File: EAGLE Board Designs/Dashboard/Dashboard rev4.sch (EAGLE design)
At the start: 97 parts, among them J1 CONNECTOR-AVR-ISP_2X05_SMD, J2 CONNECTOR-6_μF_S_RA_, J3 CONNECTOR-CAN_μF_S_RA_, J4 CONNECTOR-8_μF_S_RA_, J5 JUMPER_0603_, Q1 TRANSISTOR_N_MOS__PMV15ENEA, Q2 TRANSISTOR_N_MOS__PMV15ENEA, Q3 TRANSISTOR_N_MOS__PMV15ENEA, Q4 TRANSISTOR_N_MOS__PMV15ENEA, Q5 TRANSISTOR_N_MOS__PMV15ENEA, Q6 TRANSISTOR_N_MOS__PMV15ENEA, Q7 TRANSISTOR_N_MOS__PMV15ENEA, Q8 TRANSISTOR_N_MOS__PMV15ENEA, U1 ATMEGA328P-AU, U2 RE46C100, U3 MCP23S08, U4 MCP2562FD, U5 MCP2515, X1 CRYSTAL_16MHZ, X2 CRYSTAL_16MHZ

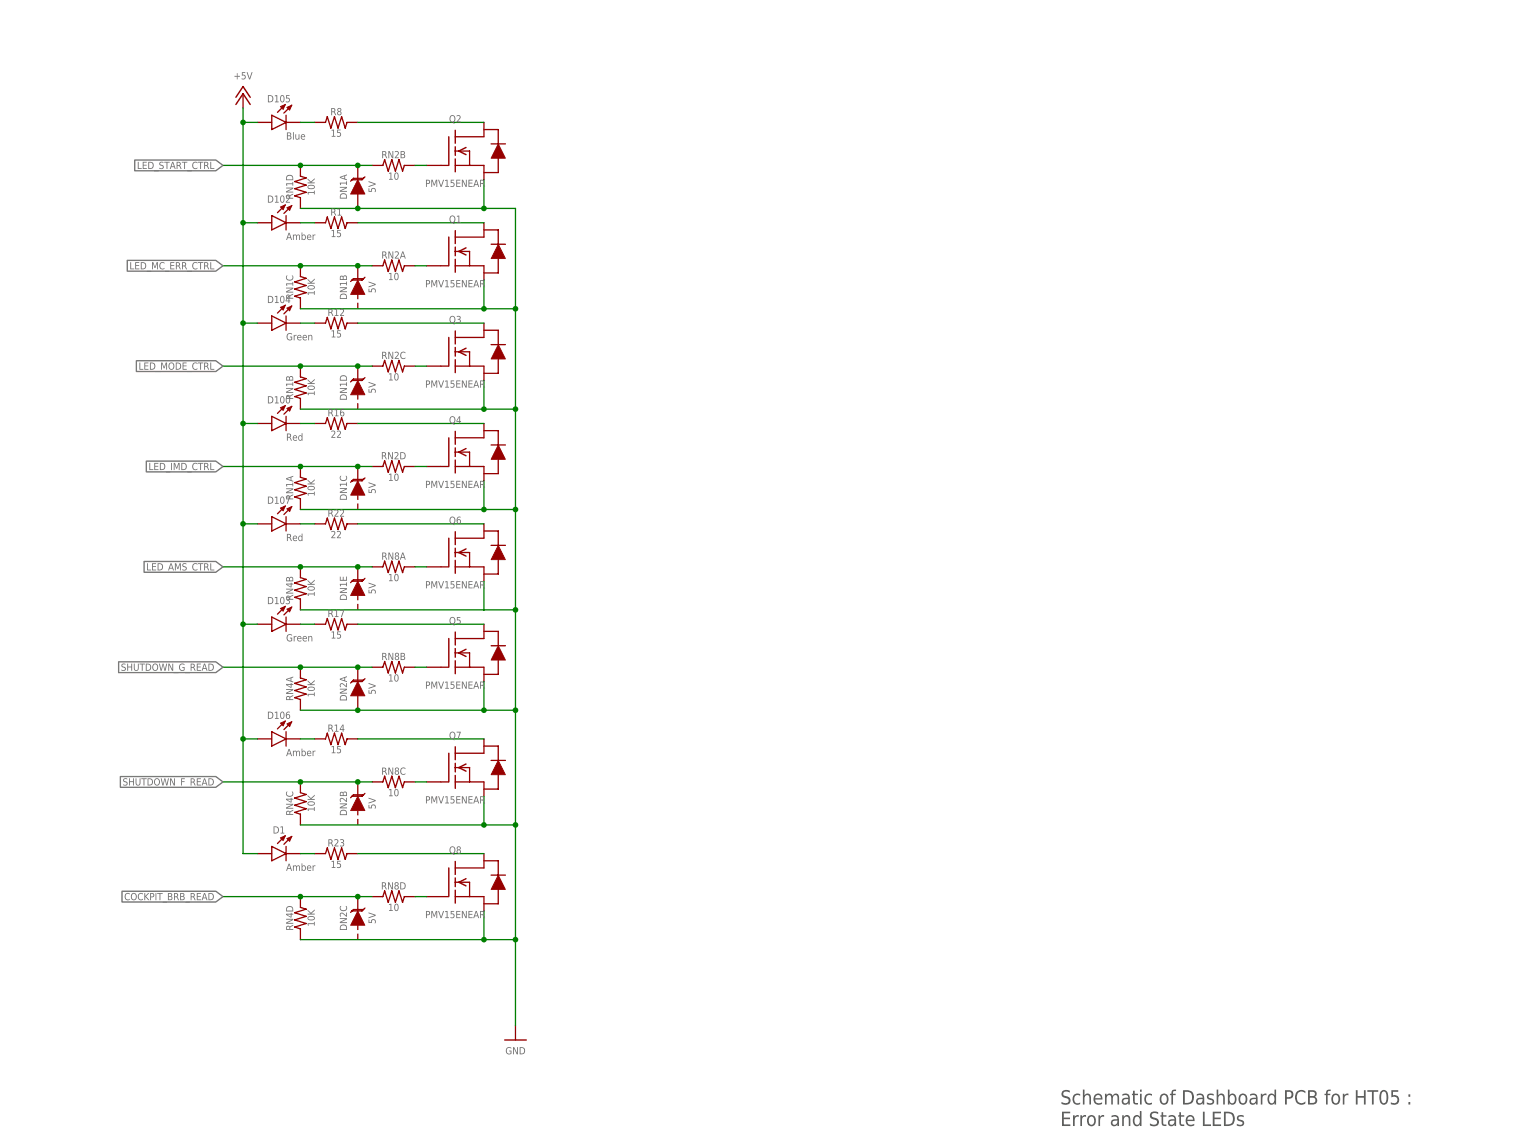
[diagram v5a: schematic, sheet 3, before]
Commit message: Updated routing and TP naming
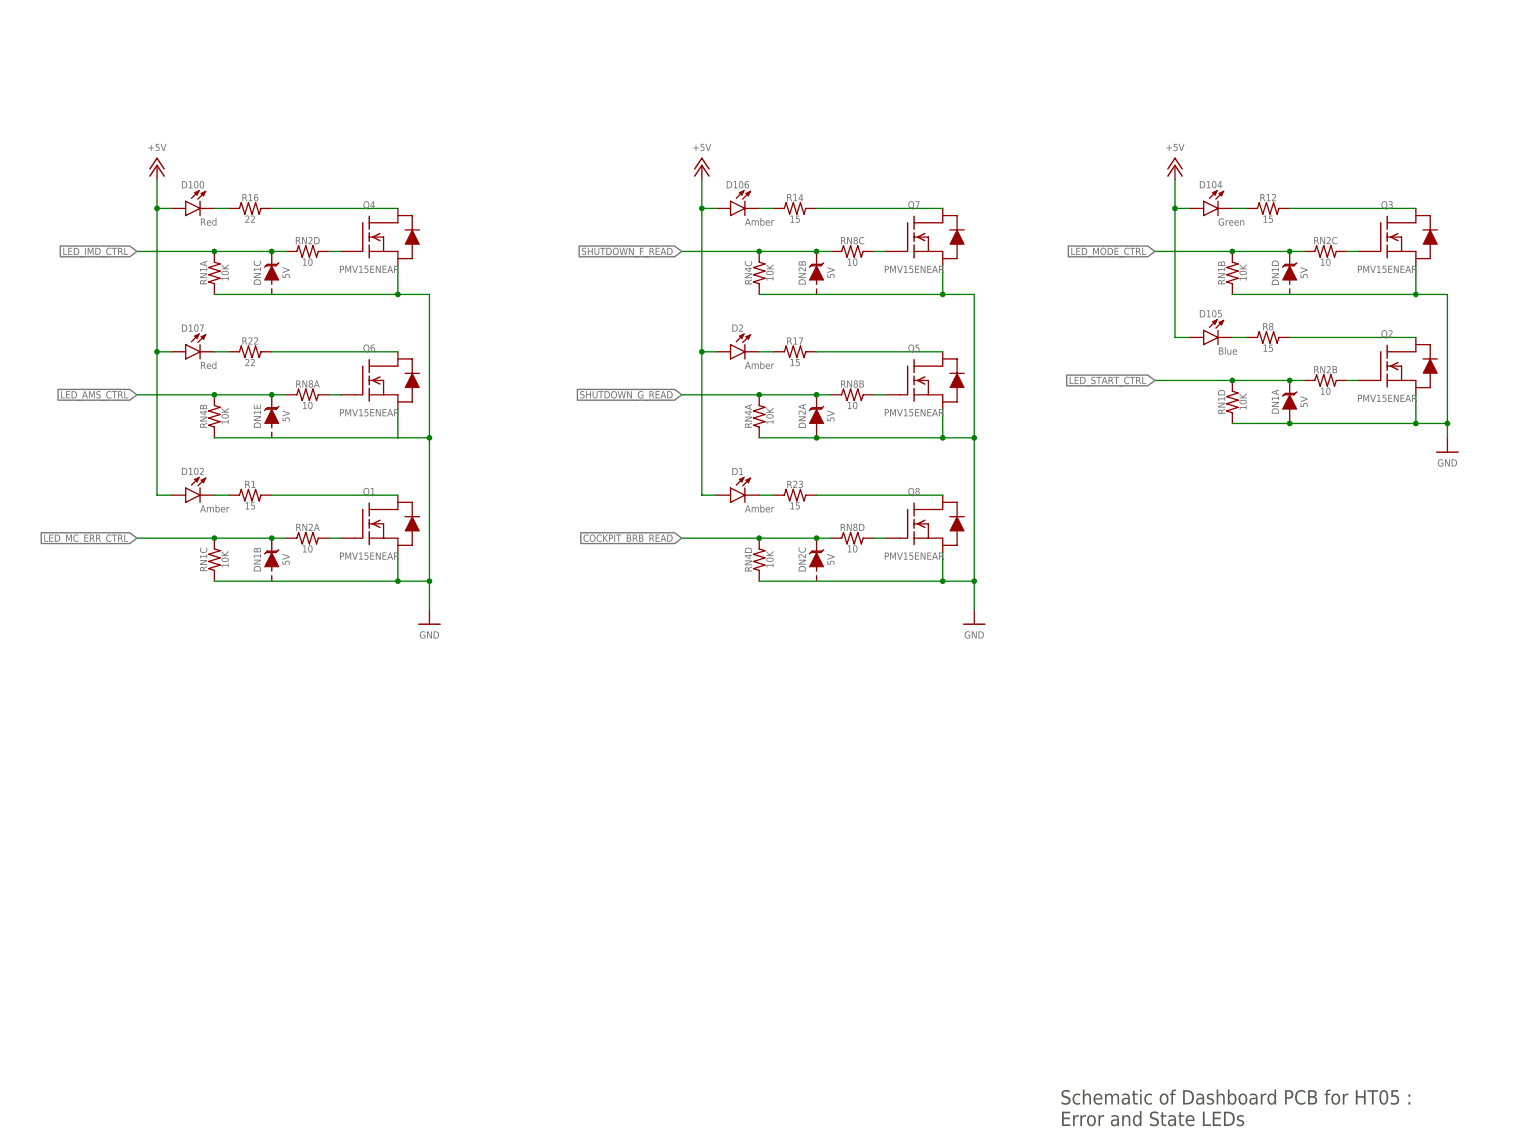
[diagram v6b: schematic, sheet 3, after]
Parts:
- removed D103: LED_2835_GREEN, HyTechDevices:LED_2835_GREEN
- added D2: LED_2835_AMBER, HyTechDevices:LED_2835_AMBER
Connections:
- net +5V: now also D2.A; no longer D103.A
- net N$40: now also D2.C; no longer D103.C
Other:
- moved on the sheet: D1, D100, D102, D104, D105, D106, D107, DN1A, DN1B, DN1C, DN1D, DN1E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

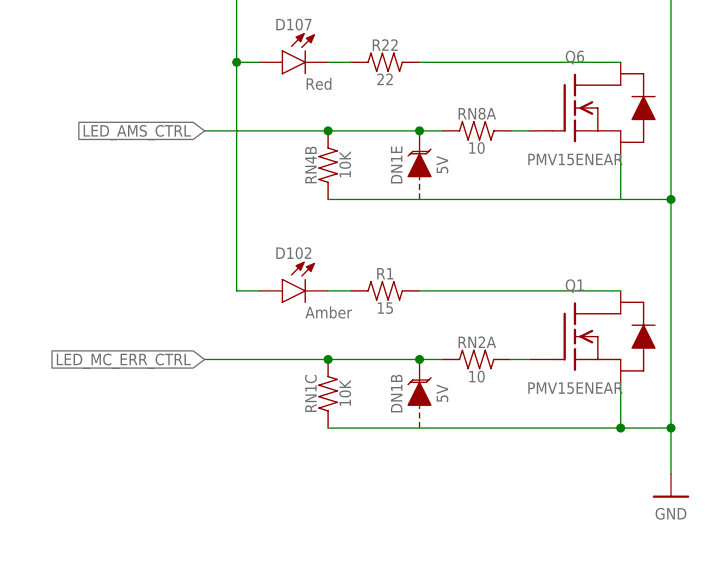
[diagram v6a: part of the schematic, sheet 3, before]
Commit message: Added red-orange led for mcu led
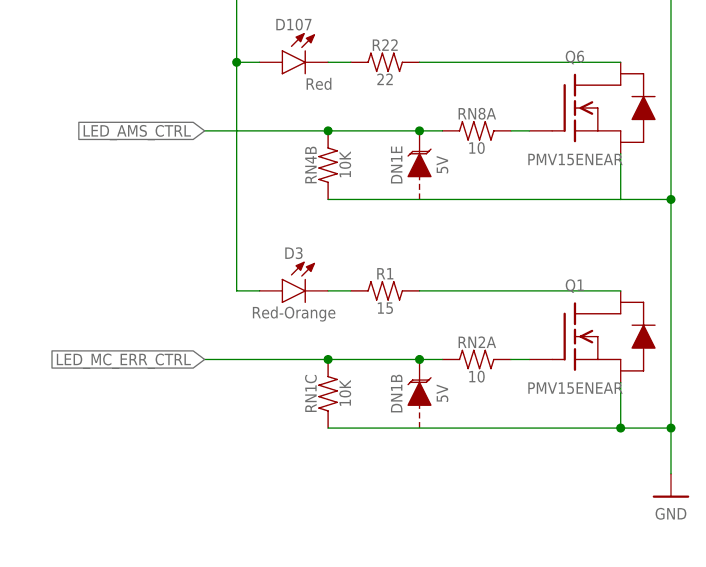
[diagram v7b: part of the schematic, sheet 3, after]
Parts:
- removed D102: LED_2835_AMBER, HyTechDevices:LED_2835_AMBER
- added D3: LED_2835_RED-ORANGE, HyTechDevices:LED_2835_RED-ORANGE
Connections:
- net +5V: now also D3.A; no longer D102.A
- net N$2: now also D3.C; no longer D102.C
- net N$41: now also J5.2; no longer J5.P$2
- net N$51: now also J5.1; no longer J5.P$1
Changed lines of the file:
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@@
 <part name="D5" library="HyTechDevices" deviceset="LED_?_*" device="0603" technology="ORANGE"/>
 <part name="RN6" library="HyTechDevices" deviceset="RESISTOR_NETWORK_4_*" device="" technology="1K"/>
-<part name="D102" library="HyTechDevices" deviceset="LED_?_*" device="2835" technology="AMBER"/>
 <part name="C10" library="HyTechDevices" deviceset="CAPACITOR_?_*" device="0603" technology="10V_0.1UF"/>
 <part name="C11" library="HyTechDevices" deviceset="CAPACITOR_?_*" device="0603" technology="10V_0.1UF"/>
@@
 <part name="P48" library="HyTechSupplies" deviceset="+5V" device=""/>
 <part name="P49" library="HyTechSupplies" deviceset="+5V" device=""/>
+<part name="D3" library="HyTechDevices" deviceset="LED_?_*" device="2835" technology="RED-ORANGE"/>
 </parts>
 <sheets>
@@
 <pinref part="R20" gate="G$1" pin="2"/>
 <wire x1="220.98" y1="154.94" x2="220.98" y2="152.4" width="0.1524" layer="91"/>
-<pinref part="J5" gate="G$1" pin="P$1"/>
+<pinref part="J5" gate="G$1" pin="1"/>
 </segment>
 </net>
@@
 <junction x="220.98" y="165.1"/>
 <pinref part="U4" gate="G$1" pin="RXD"/>
-<pinref part="J5" gate="G$1" pin="P$2"/>
+<pinref part="J5" gate="G$1" pin="2"/>
 </segment>
 </net>
@@
 <attribute name="RESISTANCE" x="158.75" y="140.97" size="1.27" layer="96" align="top-center"/>
 </instance>
-<instance part="D102" gate="LED" x="43.18" y="124.46" smashed="yes">
-<attribute name="COLOR" x="43.18" y="122.682" size="1.27" layer="95" align="top-left"/>
-<attribute name="NAME" x="41.91" y="128.016" size="1.27" layer="96" align="bottom-center"/>
-</instance>
 <instance part="DN1" gate="E" x="55.88" y="139.7" smashed="yes" rot="R90">
 <attribute name="NAME" x="53.975" y="138.43" size="1.27" layer="95" rot="R90" align="bottom-center"/>
@@
 <instance part="P49" gate="1" x="215.9" y="182.88" smashed="yes">
 <attribute name="VALUE" x="215.9" y="185.42" size="1.27" layer="96" align="bottom-center"/>
+</instance>
+<instance part="D3" gate="LED" x="43.18" y="124.46" smashed="yes">
+<attribute name="COLOR" x="41.91" y="122.682" size="1.27" layer="95" align="top-center"/>
+<attribute name="NAME" x="41.91" y="128.016" size="1.27" layer="96" align="bottom-center"/>
 </instance>
 </instances>
@@
 <segment>
 <wire x1="48.26" y1="124.46" x2="45.72" y2="124.46" width="0.1524" layer="91"/>
-<pinref part="D102" gate="LED" pin="C"/>
 <pinref part="R1" gate="G$1" pin="1"/>
+<pinref part="D3" gate="LED" pin="C"/>
 </segment>
 </net>
@@
 <wire x1="35.56" y1="175.26" x2="35.56" y2="149.86" width="0.1524" layer="91"/>
 <junction x="35.56" y="175.26"/>
-<pinref part="D102" gate="LED" pin="A"/>
 <wire x1="38.1" y1="124.46" x2="35.56" y2="124.46" width="0.1524" layer="91"/>
 <wire x1="35.56" y1="149.86" x2="35.56" y2="124.46" width="0.1524" layer="91"/>
 <junction x="35.56" y="149.86"/>
-</segment>
-<segment>
+<pinref part="D3" gate="LED" pin="A"/>
+</segment>
+<segment>

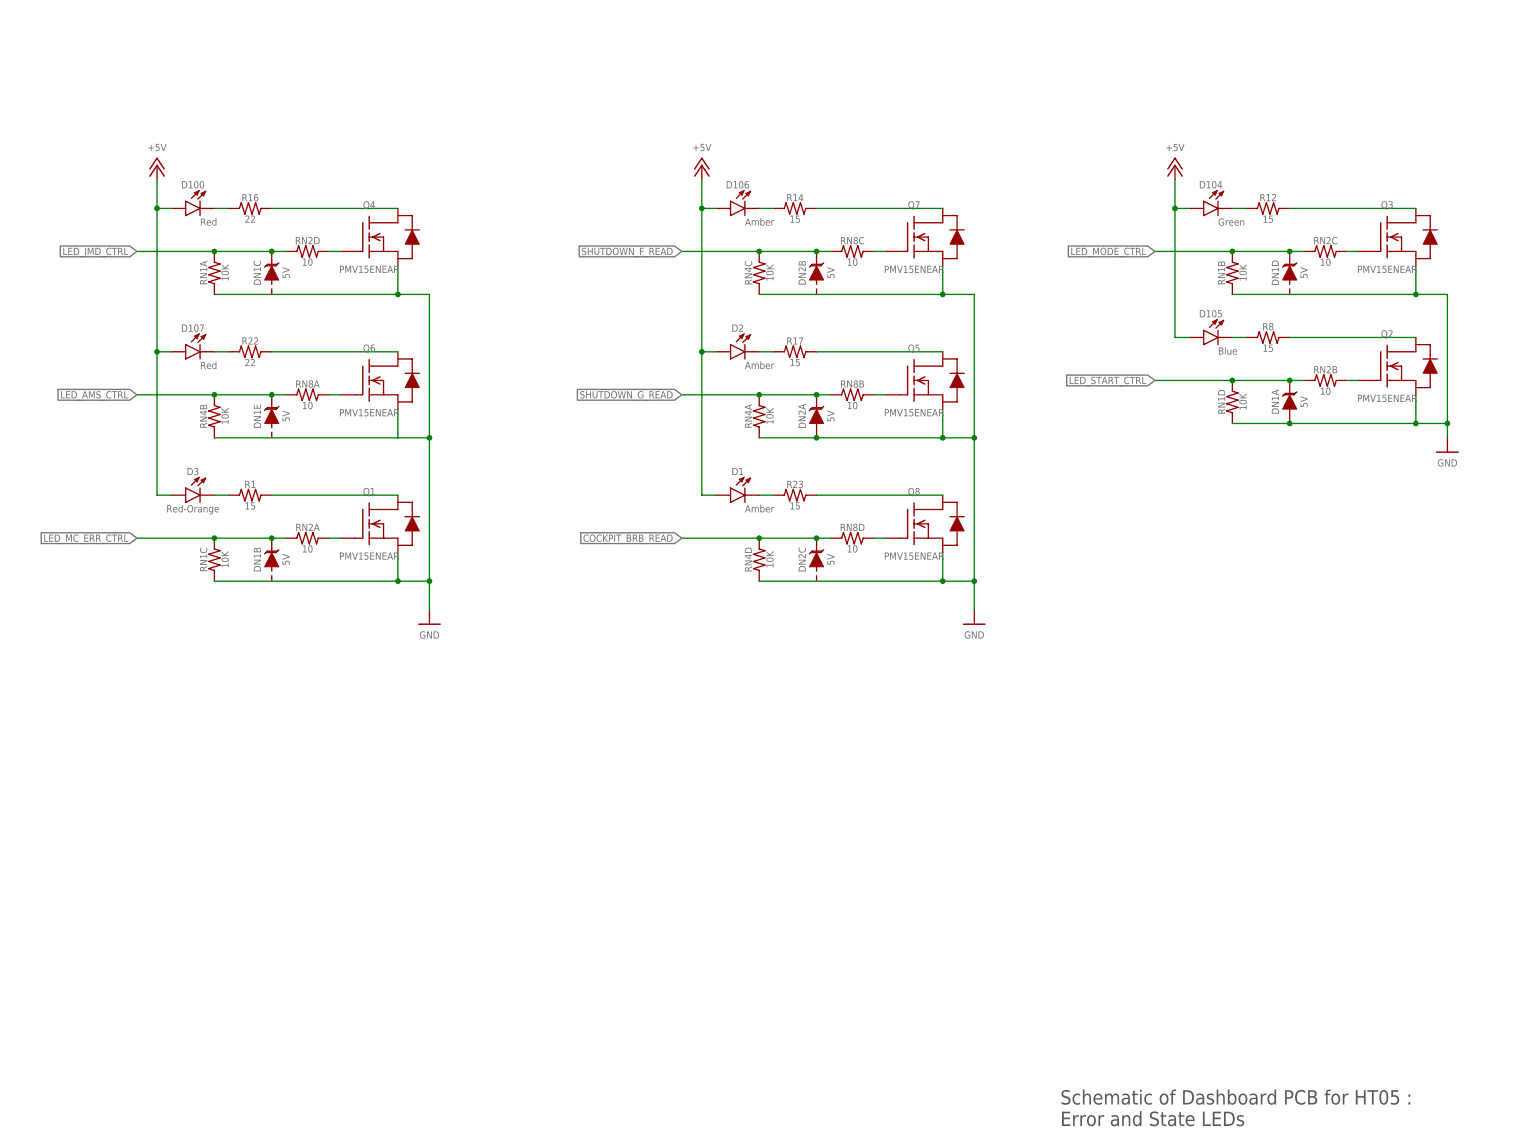
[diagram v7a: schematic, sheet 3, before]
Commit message: Added not gates and tractive LED
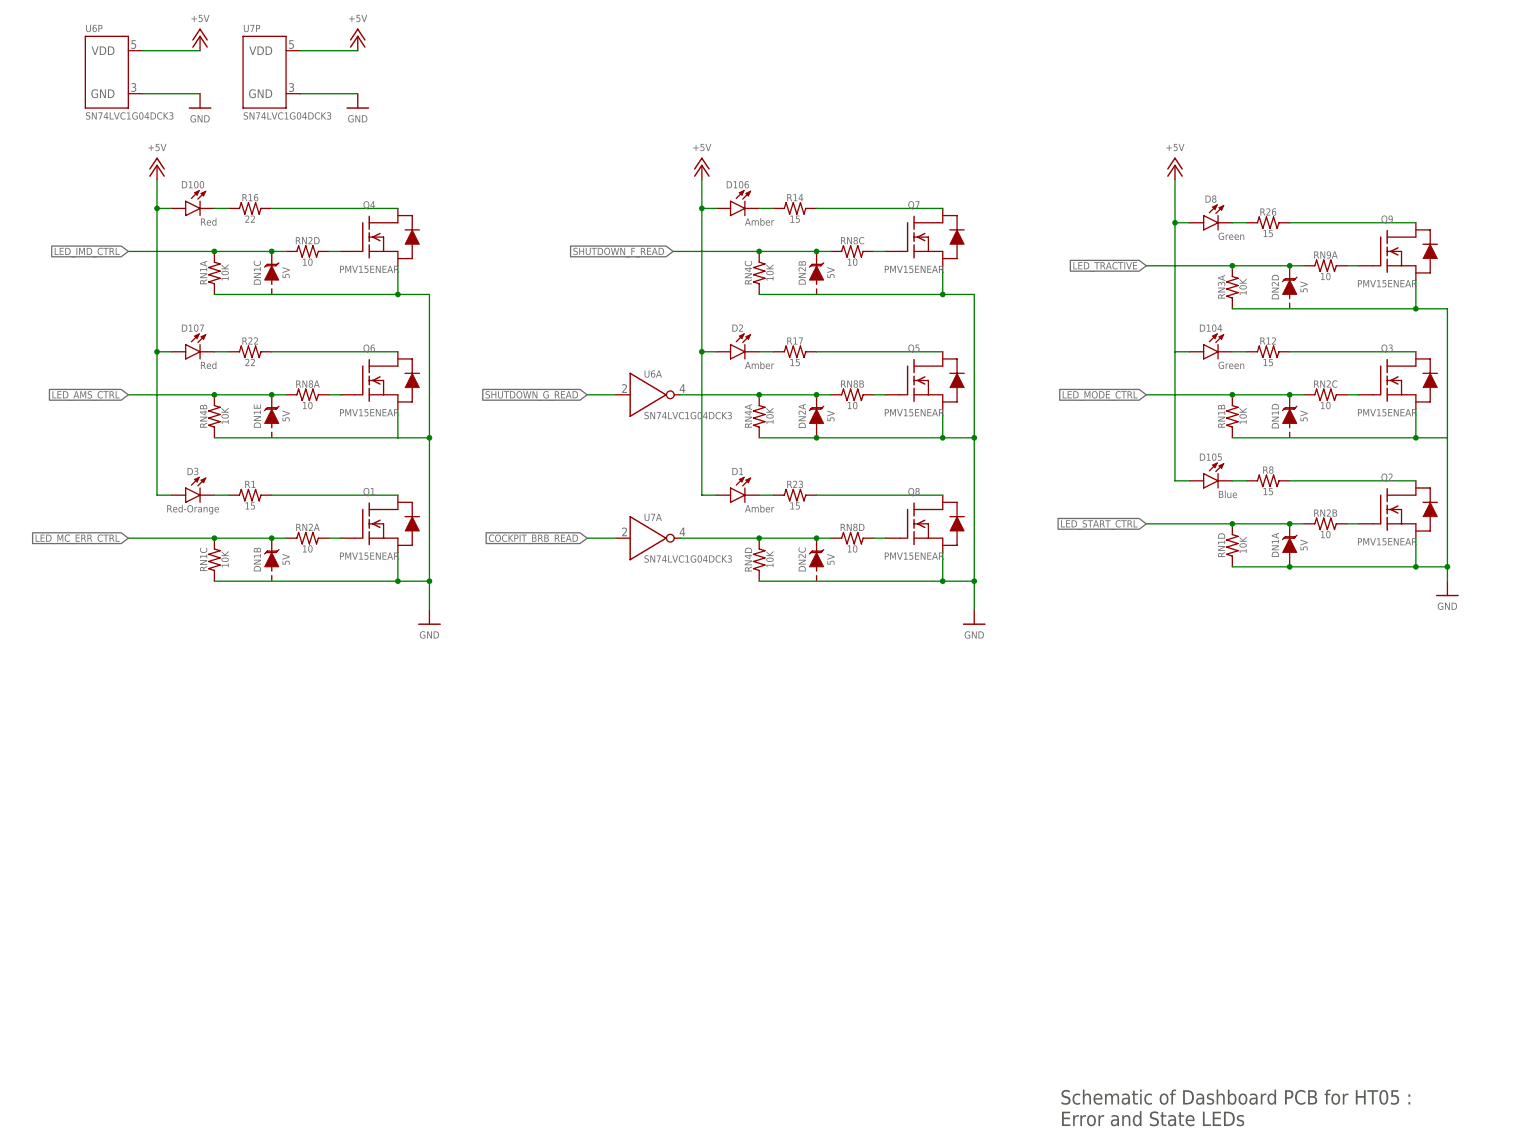
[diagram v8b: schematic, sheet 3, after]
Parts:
- added D8: LED_2835_GREEN, HyTechDevices:LED_2835_GREEN
- added Q9: TRANSISTOR_N_MOS__PMV15ENEA, HyTechDevices:TRANSISTOR_N_MOS__PMV15ENEA
- added R26: RESISTOR_0603_15, HyTechDevices:RESISTOR_0603_15
- added RN3: RESISTOR_NETWORK_4_10K, HyTechDevices:RESISTOR_NETWORK_4_10K
- added RN9: RESISTOR_NETWORK_4_10, HyTechDevices:RESISTOR_NETWORK_4_10
- added U6, U7: LOGICGATE_INVERTER_DCK3, HyTechDevices:LOGICGATE_INVERTER_DCK3
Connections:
- new net GND1: DN1A.A, Q2.S, Q3.S, Q9.S, RN1B.1, RN1D.1, RN3A.1
- new net LED_TRACTIVE: DN2D.C, RN3A.2, RN9A.1, U1.19(A5)
- new net N$32: D104.A, D105.A, D8.A
- new net N$33: D8.C, R26.1
- new net N$45: Q9.D, R26.2
- new net N$47: Q9.G, RN9A.2
- new net N$48: DN2A.C, RN4A.2, RN8B.1, U6A.!IN
- new net N$56: DN2C.C, RN4D.2, RN8D.1, U7A.!IN
- net +5V: now also U6P.VDD, U7P.VDD; no longer D104.A, D105.A
- net COCKPIT_BRB_READ: now also U7A.IN; no longer DN2C.C, RN4D.2, RN8D.1
- net GND: now also U6P.GND, U7P.GND; no longer DN1A.A, Q2.S, Q3.S, RN1B.1, RN1D.1
- net SHUTDOWN_G_READ: now also U6A.IN; no longer DN2A.C, RN4A.2, RN8B.1
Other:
- moved on the sheet: D104, D105, DN1A, DN1D, Q2, Q3, R11, R12, R8, RN1B, RN1D, RN2B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
